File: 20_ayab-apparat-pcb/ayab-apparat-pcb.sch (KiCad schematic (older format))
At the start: 9 parts, among them J1 JACK_2P, P10 CONN_2, U1 7805

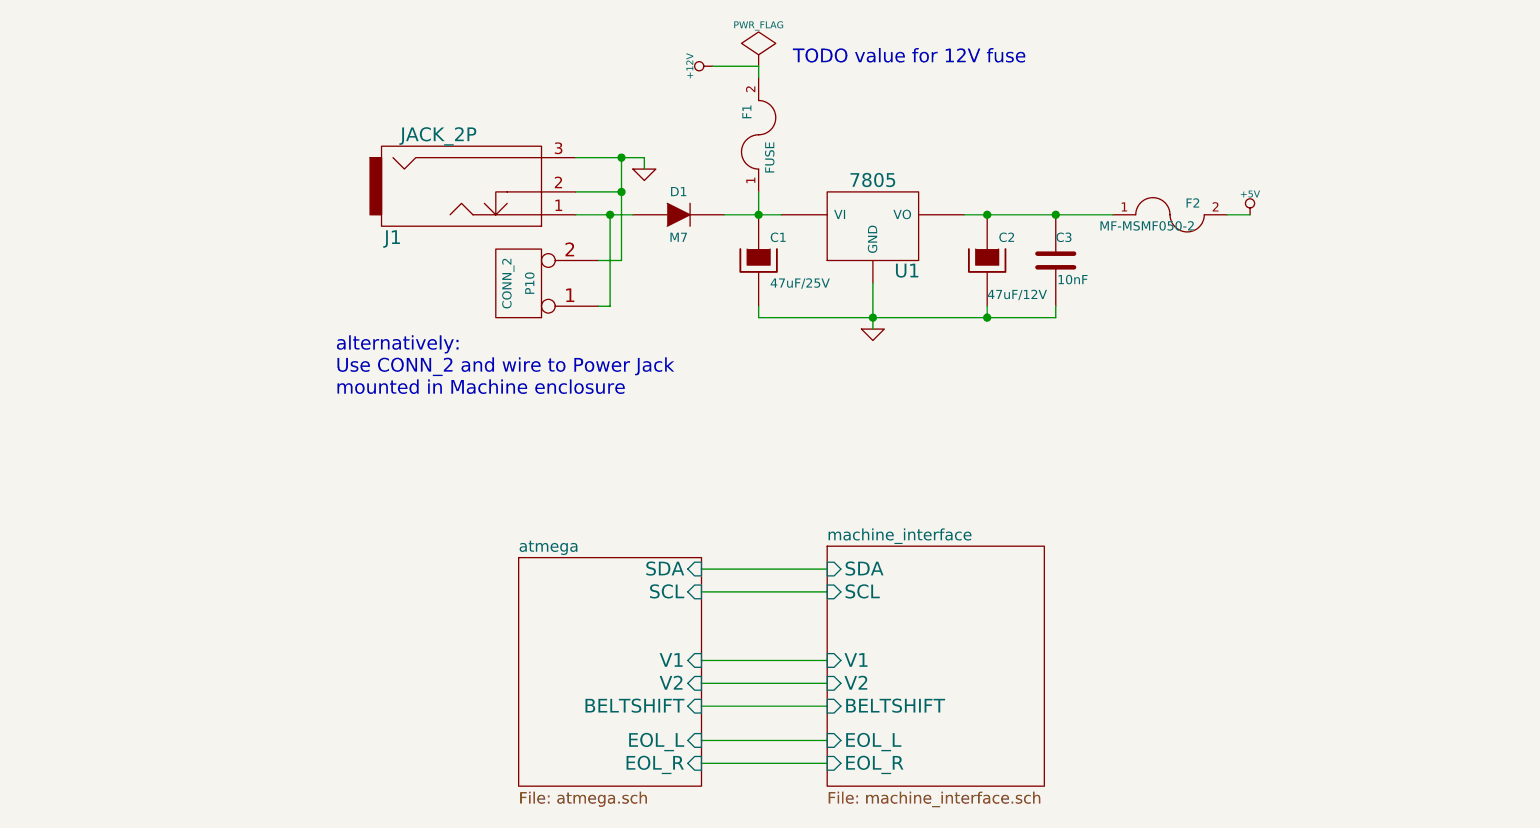
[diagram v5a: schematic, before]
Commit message: Added Packages and minor changes in schematic
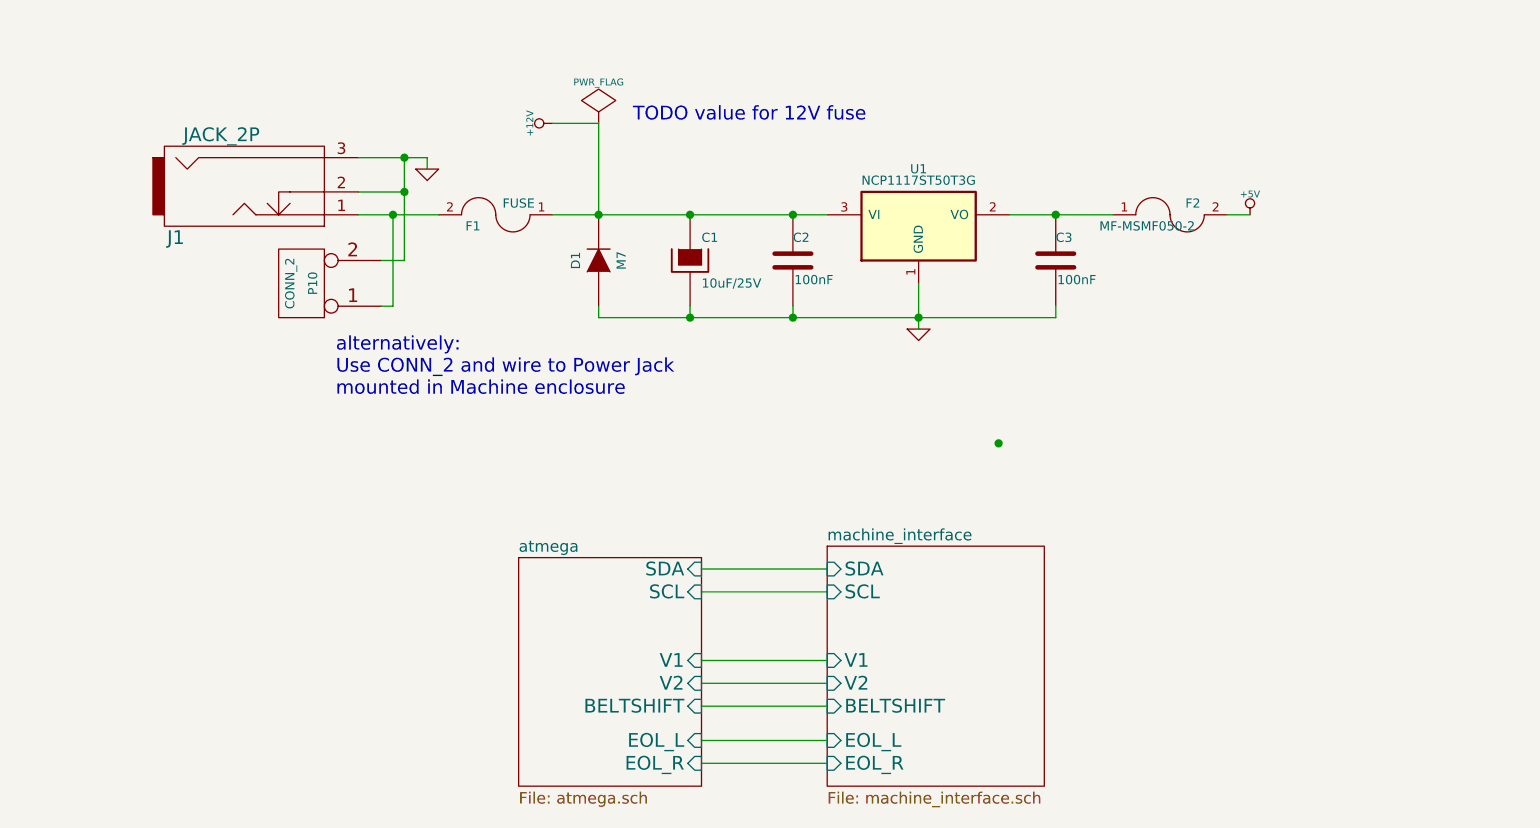
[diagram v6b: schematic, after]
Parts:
- removed C2: 47uF/12V, symbol CAPAPOL
- removed U1: 7805, symbol 7805
- added C2: 100nF, symbol C
- added U1: NCP1117ST50T3G, symbol NCP1117ST50T3G
- C1: value 47uF/25V -> 10uF/25V
- C3: value 10nF -> 100nF
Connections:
- net +12V: now also C1.1, D1.2 (K), F1.1, C2.1, U1.3 (VI); no longer F1.2
- net GND: now also D1.1 (A), C2.2, U1.1 (GND)
- net at J1.1, P10.1 (P1): now also F1.2; no longer D1.1 (A)
- net at C3.1, F2.1: now also U1.2 (VO)
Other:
- moved on the sheet: C1, D1, F1, J1, P10
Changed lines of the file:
@@
 F8 "EOL_L" I R 5450 4600 60
 $EndSheet
-Wire Wire Line
-	5450 4250 6000 4250
-Wire Wire Line
-	5450 4350 6000 4350
-Wire Wire Line
-	5450 4450 6000 4450
-Wire Wire Line
-	5450 3950 6000 3950
-Wire Wire Line
-	5450 3850 6000 3850
-Wire Wire Line
-	5450 4600 6000 4600
-Wire Wire Line
-	5450 4700 6000 4700
 $Comp
 L JACK_2P J1
 U 1 1 52EAACEF
-P 4450 2200
-F 0 "J1" H 4100 2000 60  0000 C CNN
-F 1 "JACK_2P" H 4300 2450 60  0000 C CNN
-F 2 "" H 4450 2200 60  0000 C CNN
-F 3 "" H 4450 2200 60  0000 C CNN
-	1    4450 2200
+P 3500 2200
+F 0 "J1" H 3150 2000 60  0000 C CNN
+F 1 "JACK_2P" H 3350 2450 60  0000 C CNN
+F 2 "" H 3500 2200 60  0000 C CNN
+F 3 "" H 3500 2200 60  0000 C CNN
+	1    3500 2200
 	1    0    0    -1
 $EndComp
@@
 L CAPAPOL C1
 U 1 1 52EAB7DE
-P 5700 2500
-F 0 "C1" H 5750 2600 40  0000 L CNN
-F 1 "47uF/25V" H 5750 2400 40  0000 L CNN
-F 2 "" H 5800 2350 30  0000 C CNN
-F 3 "" H 5700 2500 300 0000 C CNN
-	1    5700 2500
-	1    0    0    -1
-$EndComp
-$Comp
-L 7805 U1
-U 1 1 52EAB846
-P 6200 2350
-F 0 "U1" H 6350 2154 60  0000 C CNN
-F 1 "7805" H 6200 2550 60  0000 C CNN
-F 2 "" H 6200 2350 60  0000 C CNN
-F 3 "" H 6200 2350 60  0000 C CNN
-	1    6200 2350
-	1    0    0    -1
-$EndComp
-$Comp
-L CAPAPOL C2
-U 1 1 52EAB85A
-P 6700 2500
-F 0 "C2" H 6750 2600 40  0000 L CNN
-F 1 "47uF/12V" H 6700 2350 40  0000 L CNN
-F 2 "" H 6800 2350 30  0000 C CNN
-F 3 "" H 6700 2500 300 0000 C CNN
-	1    6700 2500
+P 5400 2500
+F 0 "C1" H 5450 2600 40  0000 L CNN
+F 1 "10uF/25V" H 5450 2400 40  0000 L CNN
+F 2 "" H 5500 2350 30  0000 C CNN
+F 3 "" H 5400 2500 300 0000 C CNN
+	1    5400 2500
 	1    0    0    -1
 $EndComp
@@
 L DIODE D1
 U 1 1 52EAB86E
-P 5350 2300
-F 0 "D1" H 5350 2400 40  0000 C CNN
-F 1 "M7" H 5350 2200 40  0000 C CNN
-F 2 "" H 5350 2300 60  0000 C CNN
-F 3 "" H 5350 2300 60  0000 C CNN
-	1    5350 2300
-	1    0    0    -1
-$EndComp
-Wire Wire Line
-	4900 2200 5100 2200
-Wire Wire Line
-	5100 2050 5100 2500
-Wire Wire Line
-	4900 2050 5200 2050
-Wire Wire Line
-	4900 2300 5150 2300
+P 5000 2500
+F 0 "D1" H 5000 2600 40  0000 C CNN
+F 1 "M7" H 5000 2400 40  0000 C CNN
+F 2 "" H 5000 2500 60  0000 C CNN
+F 3 "" H 5000 2500 60  0000 C CNN
+	1    5000 2500
+	0    -1   -1   0
+$EndComp
 $Comp
 L GND #PWR01
 U 1 1 52EAB978
-P 5200 2100
-F 0 "#PWR01" H 5200 2100 30  0001 C CNN
-F 1 "GND" H 5200 2030 30  0001 C CNN
-F 2 "" H 5200 2100 60  0000 C CNN
-F 3 "" H 5200 2100 60  0000 C CNN
-	1    5200 2100
-	1    0    0    -1
-$EndComp
-Wire Wire Line
-	5200 2050 5200 2100
-Connection ~ 5100 2050
-Wire Wire Line
-	5550 2300 5800 2300
-Wire Wire Line
-	6600 2300 7250 2300
-Wire Wire Line
-	6700 2750 6700 2700
-Wire Wire Line
-	5700 2750 7000 2750
-Wire Wire Line
-	5700 2750 5700 2700
+P 4250 2100
+F 0 "#PWR01" H 4250 2100 30  0001 C CNN
+F 1 "GND" H 4250 2030 30  0001 C CNN
+F 2 "" H 4250 2100 60  0000 C CNN
+F 3 "" H 4250 2100 60  0000 C CNN
+	1    4250 2100
+	1    0    0    -1
+$EndComp
 $Comp
 L GND #PWR02
 U 1 1 52EABC97
-P 6200 2800
-F 0 "#PWR02" H 6200 2800 30  0001 C CNN
-F 1 "GND" H 6200 2730 30  0001 C CNN
-F 2 "" H 6200 2800 60  0000 C CNN
-F 3 "" H 6200 2800 60  0000 C CNN
-	1    6200 2800
-	1    0    0    -1
-$EndComp
-Wire Wire Line
-	6200 2600 6200 2800
-Connection ~ 6200 2750
+P 6400 2800
+F 0 "#PWR02" H 6400 2800 30  0001 C CNN
+F 1 "GND" H 6400 2730 30  0001 C CNN
+F 2 "" H 6400 2800 60  0000 C CNN
+F 3 "" H 6400 2800 60  0000 C CNN
+	1    6400 2800
+	1    0    0    -1
+$EndComp
 $Comp
 L C C3
@@
 P 7000 2500
 F 0 "C3" H 7000 2600 40  0000 L CNN
-F 1 "10nF" H 7006 2415 40  0000 L CNN
+F 1 "100nF" H 7006 2415 40  0000 L CNN
 F 2 "" H 7038 2350 30  0000 C CNN
 F 3 "" H 7000 2500 60  0000 C CNN
@@
 	1    0    0    -1
 $EndComp
-Connection ~ 6700 2300
-Connection ~ 7000 2300
-Wire Wire Line
-	7000 2750 7000 2700
-Connection ~ 6700 2750
 $Comp
 L +5V #PWR03
@@
 L +12V #PWR04
 U 1 1 52EAEFAF
-P 5500 1650
-F 0 "#PWR04" H 5500 1600 20  0001 C CNN
-F 1 "+12V" H 5500 1750 30  0000 C CNN
-F 2 "" H 5500 1650 60  0000 C CNN
-F 3 "" H 5500 1650 60  0000 C CNN
-	1    5500 1650
+P 4800 1900
+F 0 "#PWR04" H 4800 1850 20  0001 C CNN
+F 1 "+12V" H 4800 2000 30  0000 C CNN
+F 2 "" H 4800 1900 60  0000 C CNN
+F 3 "" H 4800 1900 60  0000 C CNN
+	1    4800 1900
 	0    -1   -1   0
 $EndComp
@@
 	1    0    0    -1
 $EndComp
-Wire Wire Line
-	7750 2300 7850 2300
 $Comp
 L FUSE F1
 U 1 1 52EAF592
-P 5700 1950
-F 0 "F1" H 5800 2000 40  0000 C CNN
-F 1 "FUSE" H 5600 1900 40  0000 C CNN
-F 2 "" H 5700 1950 60  0000 C CNN
-F 3 "" H 5700 1950 60  0000 C CNN
-	1    5700 1950
-	0    -1   -1   0
-$EndComp
-Wire Wire Line
-	5700 2300 5700 2200
-Connection ~ 5700 2300
+P 4550 2300
+F 0 "F1" H 4650 2350 40  0000 C CNN
+F 1 "FUSE" H 4450 2250 40  0000 C CNN
+F 2 "" H 4550 2300 60  0000 C CNN
+F 3 "" H 4550 2300 60  0000 C CNN
+	1    4550 2300
+	-1   0    0    1
+$EndComp
 Text Notes 3850 3100 0    60   ~ 0
 alternatively:\nUse CONN_2 and wire to Power Jack\nmounted in Machine enclosure
@@
 L CONN_2 P10
 U 1 1 52EEC1AF
-P 4650 2600
-F 0 "P10" V 4600 2600 40  0000 C CNN
-F 1 "CONN_2" V 4700 2600 40  0000 C CNN
-F 2 "" H 4650 2600 60  0000 C CNN
-F 3 "" H 4650 2600 60  0000 C CNN
-	1    4650 2600
+P 3700 2600
+F 0 "P10" V 3650 2600 40  0000 C CNN
+F 1 "CONN_2" V 3750 2600 40  0000 C CNN
+F 2 "" H 3700 2600 60  0000 C CNN
+F 3 "" H 3700 2600 60  0000 C CNN
+	1    3700 2600
 	-1   0    0    1
 $EndComp
-Connection ~ 5100 2200
-Wire Wire Line
-	5100 2500 5000 2500
-Wire Wire Line
-	5000 2700 5050 2700
-Wire Wire Line
-	5050 2700 5050 2300
-Connection ~ 5050 2300
-Text Notes 5850 1650 0    60   ~ 0
+Text Notes 5150 1900 0    60   ~ 0
 TODO value for 12V fuse
-Wire Wire Line
-	5700 1700 5700 1650
-Wire Wire Line
-	5700 1650 5500 1650
 $Comp
 L PWR_FLAG #FLG05
 U 1 1 52EECA32
-P 5700 1650
-F 0 "#FLG05" H 5700 1745 30  0001 C CNN
-F 1 "PWR_FLAG" H 5700 1830 30  0000 C CNN
-F 2 "" H 5700 1650 60  0000 C CNN
-F 3 "" H 5700 1650 60  0000 C CNN
-	1    5700 1650
-	1    0    0    -1
-$EndComp
+P 5000 1900
+F 0 "#FLG05" H 5000 1995 30  0001 C CNN
+F 1 "PWR_FLAG" H 5000 2080 30  0000 C CNN
+F 2 "" H 5000 1900 60  0000 C CNN
+F 3 "" H 5000 1900 60  0000 C CNN
+	1    5000 1900
+	1    0    0    -1
+$EndComp
+$Comp
+L C C2
+U 1 1 52F1A256
+P 5850 2500
+F 0 "C2" H 5850 2600 40  0000 L CNN
+F 1 "100nF" H 5856 2415 40  0000 L CNN
+F 2 "" H 5888 2350 30  0000 C CNN
+F 3 "" H 5850 2500 60  0000 C CNN
+	1    5850 2500
+	1    0    0    -1
+$EndComp
+$Comp
+L NCP1117ST50T3G U1
+U 1 1 52F1A2B7
+P 6400 2350
+F 0 "U1" H 6400 2600 40  0000 C CNN
+F 1 "NCP1117ST50T3G" H 6400 2550 40  0000 C CNN
+F 2 "" H 6400 2350 60  0000 C CNN
+F 3 "" H 6400 2350 60  0000 C CNN
+	1    6400 2350
+	1    0    0    -1
+$EndComp
+Wire Wire Line
+	5450 4250 6000 4250
+Wire Wire Line
+	5450 4350 6000 4350
+Wire Wire Line
+	5450 4450 6000 4450
+Wire Wire Line
+	5450 3950 6000 3950
+Wire Wire Line
+	5450 3850 6000 3850
+Wire Wire Line
+	5450 4600 6000 4600
+Wire Wire Line
+	5450 4700 6000 4700
+Wire Wire Line
+	3950 2200 4150 2200
+Wire Wire Line
+	4150 2050 4150 2500
+Wire Wire Line
+	3950 2050 4250 2050
+Wire Wire Line
+	3950 2300 4300 2300
+Wire Wire Line
+	4800 2300 6000 2300
+Wire Wire Line
+	4250 2050 4250 2100
+Connection ~ 4150 2050
+Wire Wire Line
+	6800 2300 7250 2300
+Wire Wire Line
+	5000 2750 7000 2750
+Connection ~ 7000 2300
+Wire Wire Line
+	7000 2750 7000 2700
+Wire Wire Line
+	7750 2300 7850 2300
+Connection ~ 4150 2200
+Wire Wire Line
+	4150 2500 4050 2500
+Wire Wire Line
+	4050 2700 4100 2700
+Wire Wire Line
+	4100 2700 4100 2300
+Connection ~ 4100 2300
+Wire Wire Line
+	5000 1900 5000 2300
+Wire Wire Line
+	5000 1900 4800 1900
+Connection ~ 5000 2300
+Wire Wire Line
+	5000 2700 5000 2750
+Connection ~ 5400 2300
+Wire Wire Line
+	5400 2700 5400 2750
+Connection ~ 5400 2750
+Wire Wire Line
+	5850 2700 5850 2750
+Connection ~ 5850 2750
+Wire Wire Line
+	6400 2600 6400 2800
+Connection ~ 6400 2750
+Connection ~ 5850 2300
+Connection ~ 6750 3300
 $EndSCHEMATC

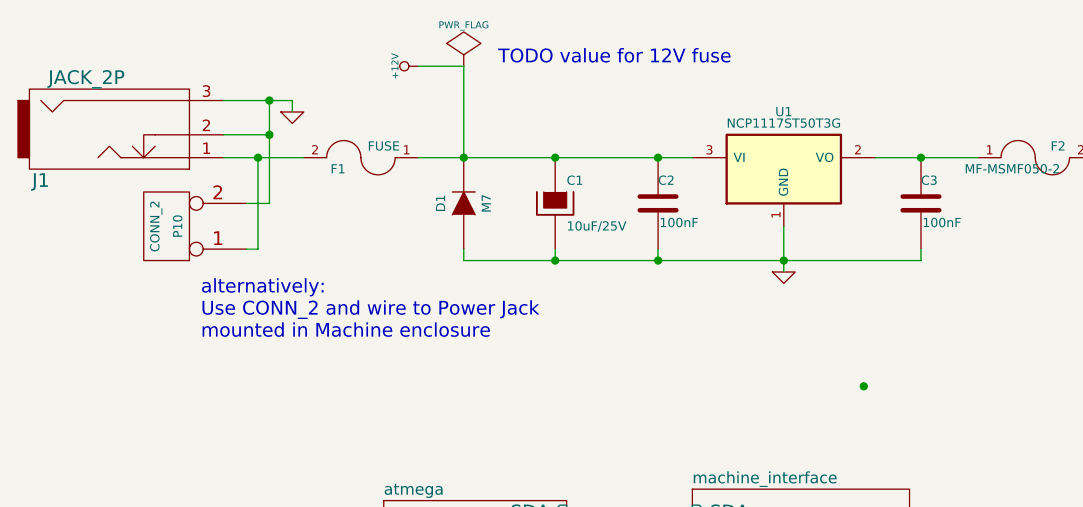
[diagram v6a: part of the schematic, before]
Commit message: added ab2tech library for SOIC18 footprint, removed DC jack in schematic TODO: Check Size of Pin Header for machine power connection
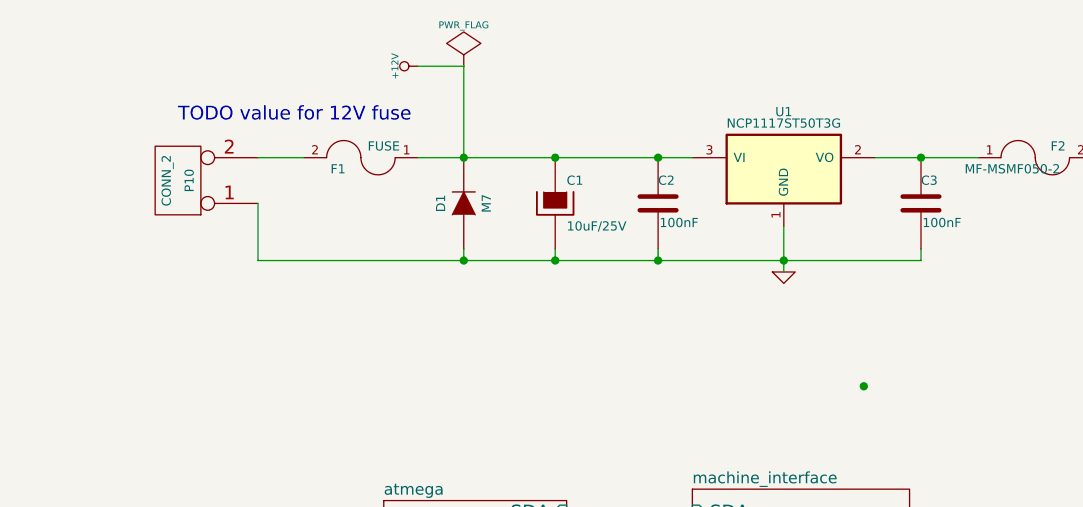
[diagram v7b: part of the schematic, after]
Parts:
- removed J1: JACK_2P, symbol JACK_2P
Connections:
- net GND: now also P10.1 (P1); no longer P10.2 (PM)
- net at F1.2: now also P10.2 (PM); no longer P10.1 (P1)
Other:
- note removed: "alternatively:\nUse CONN_2 and wire to Power Jack\nmounted in Machine enclosure"
- moved on the sheet: P10
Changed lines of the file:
@@
 $EndSheet
-$Comp
-L JACK_2P J1
-U 1 1 52EAACEF
-P 3500 2200
-F 0 "J1" H 3150 2000 60  0000 C CNN
-F 1 "JACK_2P" H 3350 2450 60  0000 C CNN
-F 2 "" H 3500 2200 60  0000 C CNN
-F 3 "" H 3500 2200 60  0000 C CNN
-	1    3500 2200
-	1    0    0    -1
-$EndComp
 $Comp
 L CAPAPOL C1
@@
 	1    5000 2500
 	0    -1   -1   0
-$EndComp
-$Comp
-L GND #PWR01
-U 1 1 52EAB978
-P 4250 2100
-F 0 "#PWR01" H 4250 2100 30  0001 C CNN
-F 1 "GND" H 4250 2030 30  0001 C CNN
-F 2 "" H 4250 2100 60  0000 C CNN
-F 3 "" H 4250 2100 60  0000 C CNN
-	1    4250 2100
-	1    0    0    -1
 $EndComp
 $Comp
@@
 	-1   0    0    1
 $EndComp
-Text Notes 3850 3100 0    60   ~ 0
-alternatively:\nUse CONN_2 and wire to Power Jack\nmounted in Machine enclosure
 $Comp
 L CONN_2 P10
 U 1 1 52EEC1AF
-P 3700 2600
-F 0 "P10" V 3650 2600 40  0000 C CNN
-F 1 "CONN_2" V 3750 2600 40  0000 C CNN
-F 2 "" H 3700 2600 60  0000 C CNN
-F 3 "" H 3700 2600 60  0000 C CNN
-	1    3700 2600
+P 3750 2400
+F 0 "P10" V 3700 2400 40  0000 C CNN
+F 1 "CONN_2" V 3800 2400 40  0000 C CNN
+F 2 "" H 3750 2400 60  0000 C CNN
+F 3 "" H 3750 2400 60  0000 C CNN
+	1    3750 2400
 	-1   0    0    1
 $EndComp
-Text Notes 5150 1900 0    60   ~ 0
+Text Notes 3750 2150 0    60   ~ 0
 TODO value for 12V fuse
 $Comp
@@
 	5450 4700 6000 4700
 Wire Wire Line
-	3950 2200 4150 2200
-Wire Wire Line
-	4150 2050 4150 2500
-Wire Wire Line
-	3950 2050 4250 2050
-Wire Wire Line
-	3950 2300 4300 2300
-Wire Wire Line
 	4800 2300 6000 2300
-Wire Wire Line
-	4250 2050 4250 2100
-Connection ~ 4150 2050
 Wire Wire Line
 	6800 2300 7250 2300
 Wire Wire Line
-	5000 2750 7000 2750
+	4100 2750 7000 2750
 Connection ~ 7000 2300
 Wire Wire Line
@@
 Wire Wire Line
 	7750 2300 7850 2300
-Connection ~ 4150 2200
-Wire Wire Line
-	4150 2500 4050 2500
-Wire Wire Line
-	4050 2700 4100 2700
-Wire Wire Line
-	4100 2700 4100 2300
-Connection ~ 4100 2300
 Wire Wire Line
 	5000 1900 5000 2300
@@
 Connection ~ 5850 2300
 Connection ~ 6750 3300
+Wire Wire Line
+	4100 2300 4300 2300
+Wire Wire Line
+	4100 2500 4100 2750
+Connection ~ 5000 2750
 $EndSCHEMATC

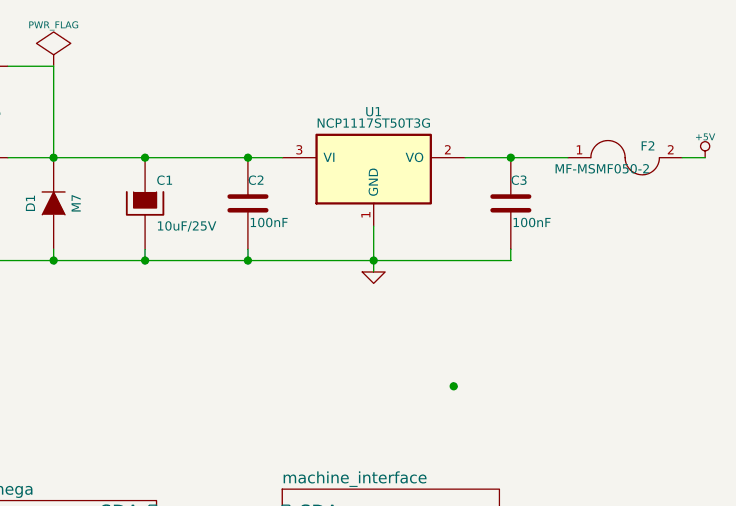
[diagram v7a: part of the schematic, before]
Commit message: initial create of layout file and BOM with some part numbers from reichelt
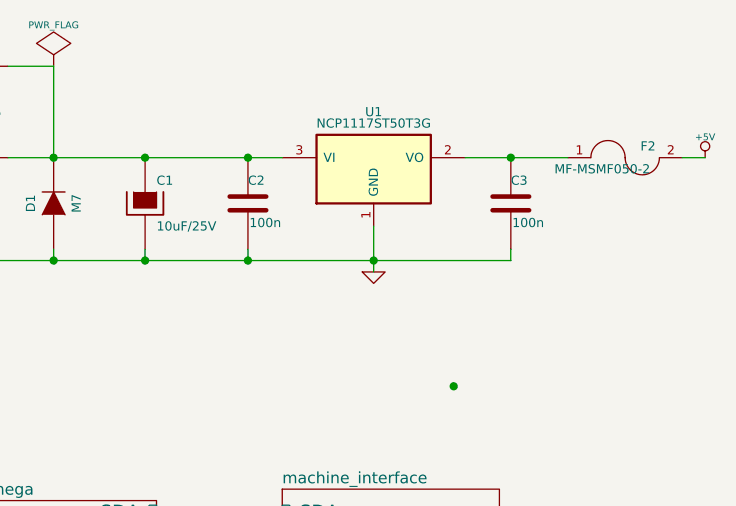
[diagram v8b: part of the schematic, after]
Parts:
- C2, C3: value 100nF -> 100n
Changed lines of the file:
@@
 P 7000 2500
 F 0 "C3" H 7000 2600 40  0000 L CNN
-F 1 "100nF" H 7006 2415 40  0000 L CNN
+F 1 "100n" H 7006 2415 40  0000 L CNN
 F 2 "" H 7038 2350 30  0000 C CNN
 F 3 "" H 7000 2500 60  0000 C CNN
@@
 P 5850 2500
 F 0 "C2" H 5850 2600 40  0000 L CNN
-F 1 "100nF" H 5856 2415 40  0000 L CNN
+F 1 "100n" H 5856 2415 40  0000 L CNN
 F 2 "" H 5888 2350 30  0000 C CNN
 F 3 "" H 5850 2500 60  0000 C CNN
